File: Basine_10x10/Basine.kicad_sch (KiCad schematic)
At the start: 55 parts, among them J1 2060-451/998-404, J10 2060-451/998-404, J11 2060-451/998-404, J12 2060-451/998-404, J13 2060-451/998-404, J14 2060-451/998-404, J15 2060-451/998-404, J16 2060-451/998-404, J2 2060-451/998-404, J3 2060-451/998-404, J4 2060-451/998-404, J5 2060-451/998-404, J6 2060-451/998-404, J7 2060-451/998-404, J8 2060-451/998-404, J9 2060-451/998-404

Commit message: passage au pas de 2,54mm pour toutes les allumettes
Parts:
- removed TP1, TP10, TP11, TP12, TP2, TP3, TP4, TP5, TP6, TP7, TP8, TP9: TestPoint, Chimere_comps:Pastille, symbol Connector:TestPoint

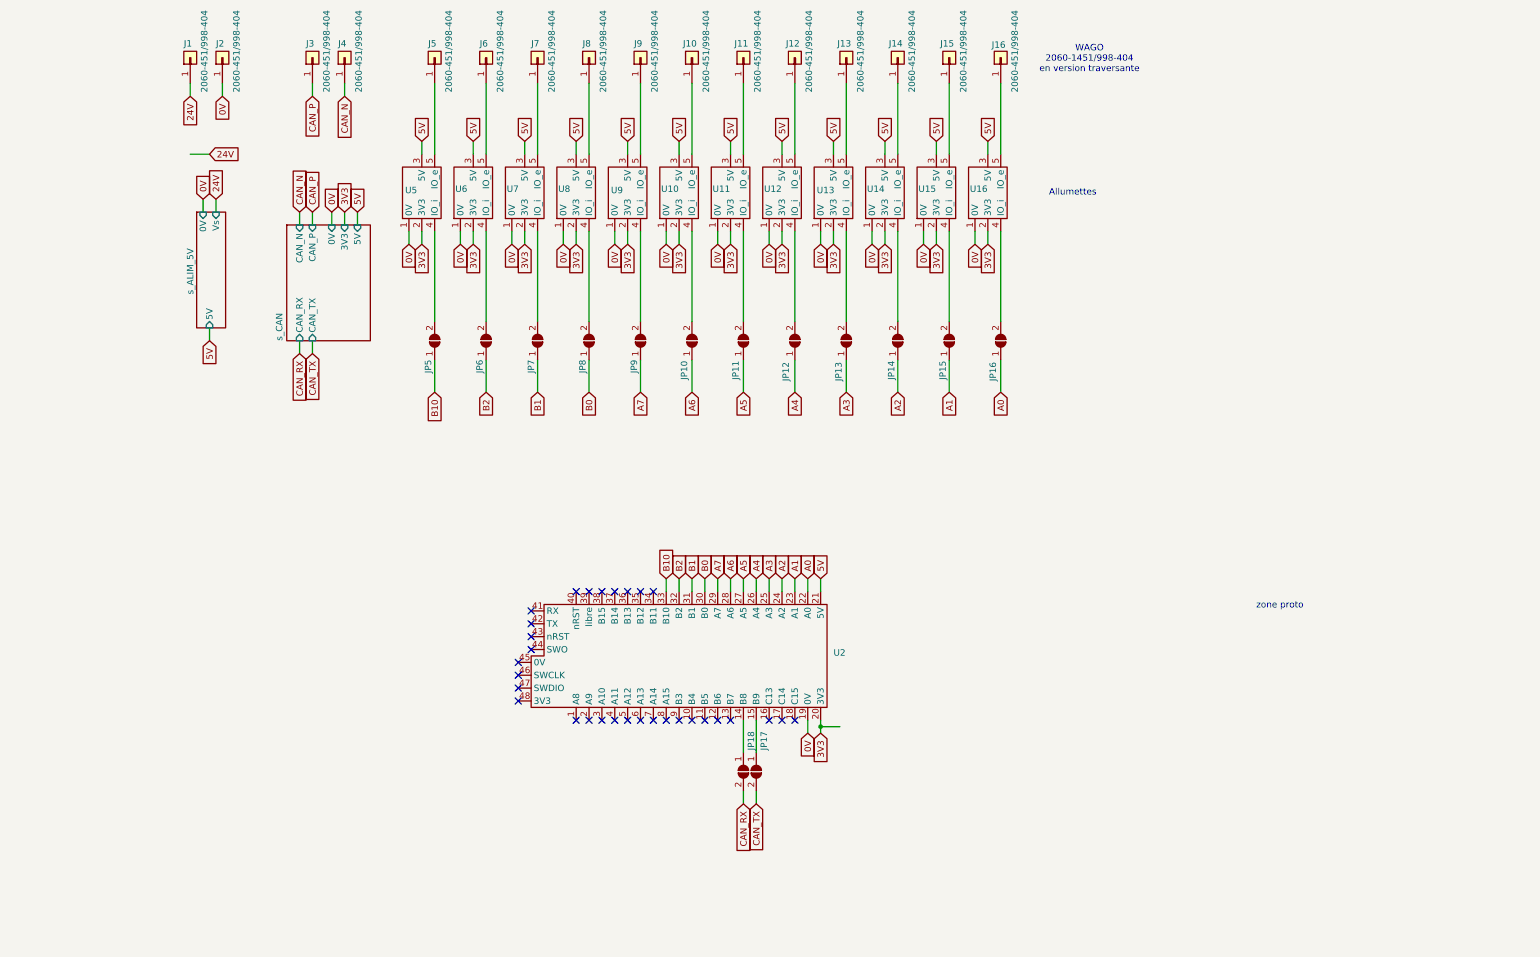
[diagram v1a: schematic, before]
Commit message: Basine 10x10 : enlever DCDC et CAN
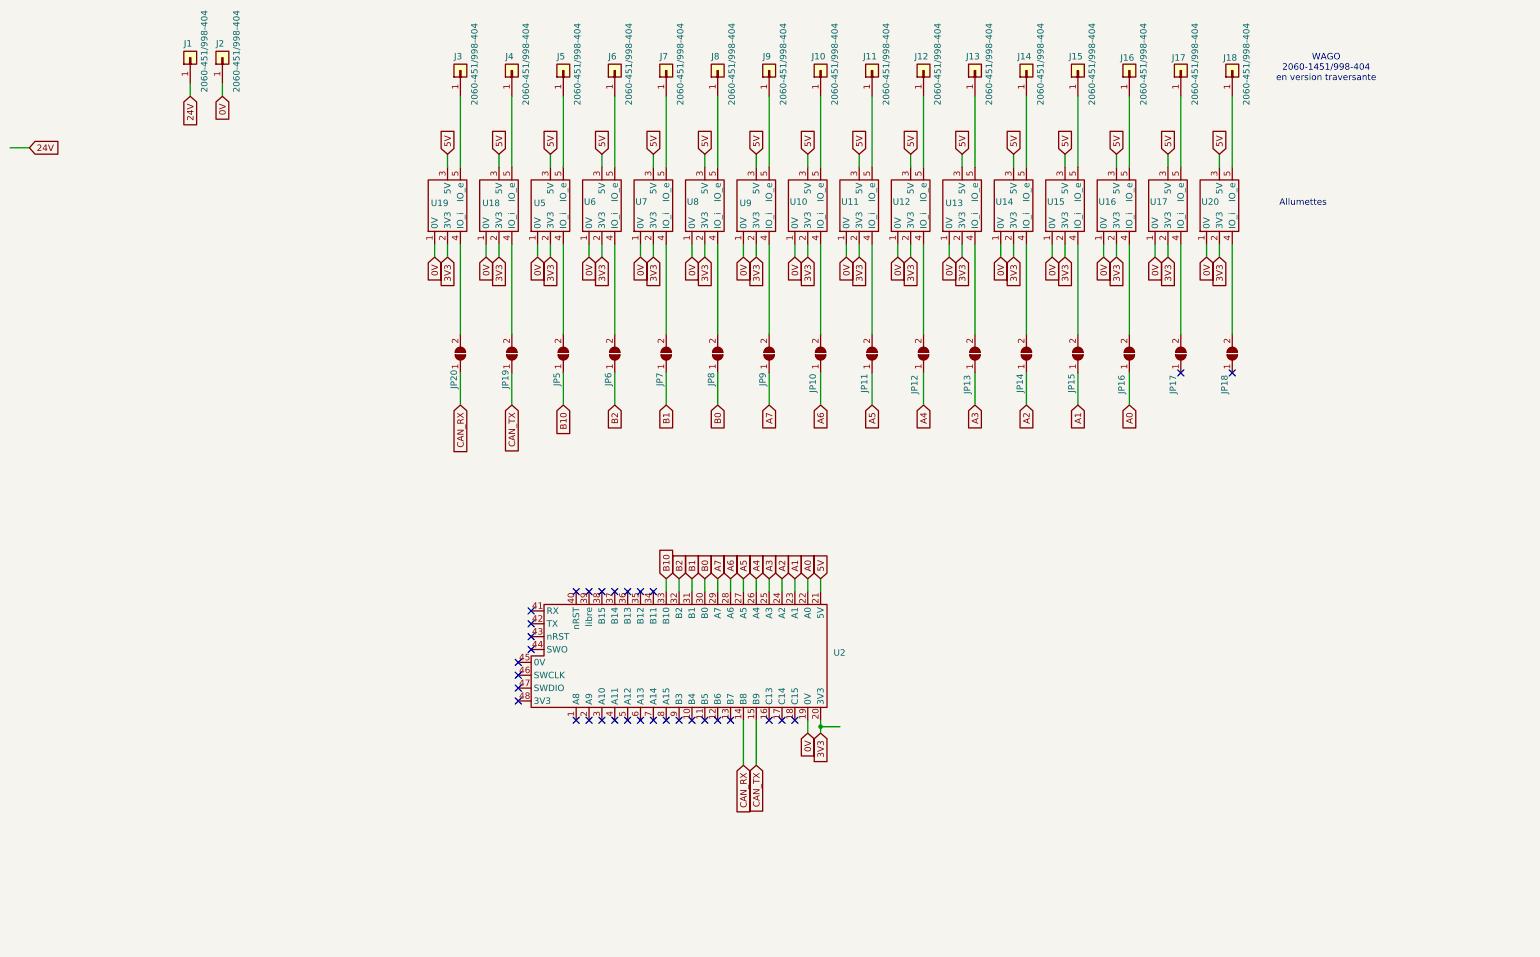
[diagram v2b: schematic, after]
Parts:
- added J17, J18: 2060-451/998-404, Chimere_comps:CONN_2060-1451_998-404_WAGO, symbol Connector_Generic:Conn_01x01
- added JP19, JP20: SolderJumper_2_Open, Jumper:SolderJumper-2_P1.3mm_Open_TrianglePad1.0x1.5mm, symbol Jumper:SolderJumper_2_Open
- added U17, U18, U19, U20: ~, Chimere_mods:Allumette, symbol Chimere_mods:Allumette
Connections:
- net 0V: now also U17.1 (0V), U18.1 (0V), U19.1 (0V), U20.1 (0V)
- net 3V3: now also U17.2 (3V3), U18.2 (3V3), U19.2 (3V3), U20.2 (3V3)
- net 5V: now also U17.3 (5V), U18.3 (5V), U19.3 (5V), U20.3 (5V)
- net CAN_RX: now also U2.14 (B8), JP20.1 (A); no longer JP18.2 (B)
- net CAN_TX: now also U2.15 (B9), JP19.1 (A); no longer JP17.2 (B)
- net at JP18.1 (A): no longer U2.14 (B8)
- net at JP17.1 (A): no longer U2.15 (B9)
- net CAN_N: no longer names the net of J4.1 (Pin_1)
- net CAN_N: now also U18.5 (IO_e)
- net CAN_P: no longer names the net of J3.1 (Pin_1)
- net CAN_P: now also U19.5 (IO_e)
- new net: JP17.2 (B), U17.4 (IO_i)
- new net: J17.1 (Pin_1), U17.5 (IO_e)
- new net: J18.1 (Pin_1), U20.5 (IO_e)
- new net: JP18.2 (B), U20.4 (IO_i)
- new net: JP20.2 (B), U19.4 (IO_i)
- new net: JP19.2 (B), U18.4 (IO_i)
- no-connect marks 31 -> 33
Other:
- removed sheet s_ALIM_5V
- removed sheet s_CAN
- note removed: "zone proto"
- moved on the sheet: J10, J11, J12, J13, J14, J15, J16, J3, J4, J5, J6, J7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

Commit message: Basine_10x10 : placement et routage
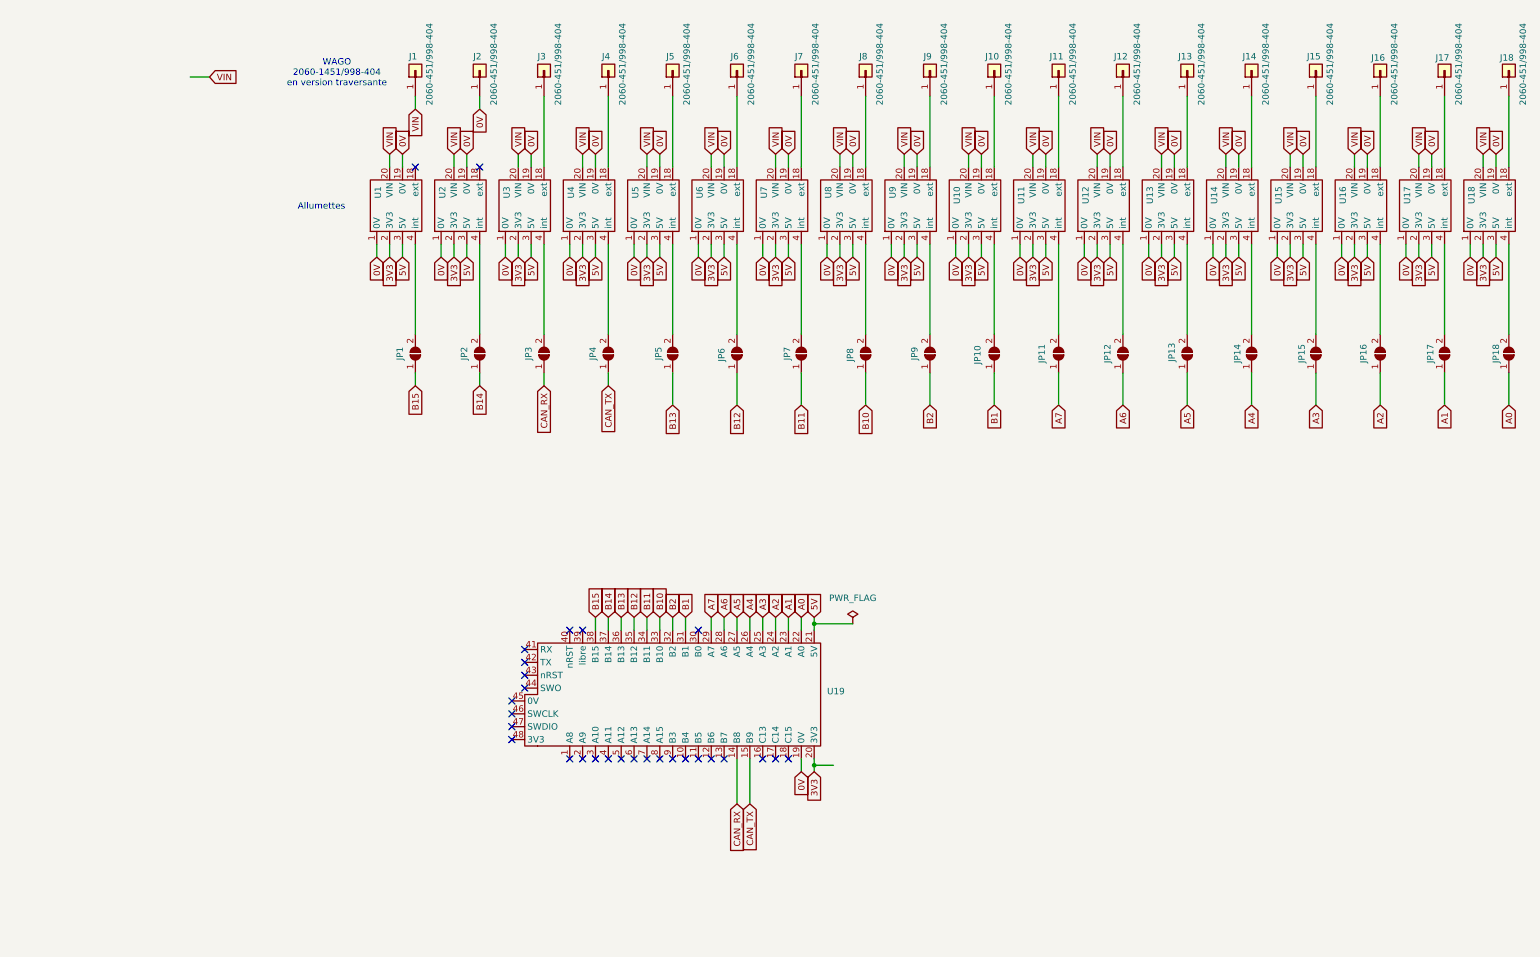
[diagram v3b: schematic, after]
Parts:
- removed U18, U19: ~, Chimere_mods:Allumette, symbol Chimere_mods:Allumette
- added JP1, JP2: SolderJumper_2_Open, Jumper:SolderJumper-2_P1.3mm_Open_TrianglePad1.0x1.5mm, symbol Jumper:SolderJumper_2_Open
- added U1, U2, U3, U4: ~, Chimere_mods:Allumette, symbol Chimere_mods:Allumette
- renumbered JP20 to JP3, JP19 to JP4, U20 to U18, U2 to U19
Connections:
- net 0V: now also U10.19 (0V), U11.19 (0V), U12.19 (0V), U13.19 (0V), U14.19 (0V), U15.19 (0V), U16.19 (0V), U17.19 (0V), U18.19 (0V), U5.19 (0V), U6.19 (0V), U7.19 (0V), U8.19 (0V), U9.19 (0V), U1.1 (0V), U1.19 (0V), U2.1 (0V), U2.19 (0V), U3.1 (0V), U3.19 (0V), U4.1 (0V), U4.19 (0V)
- net 3V3: now also U1.2 (3V3), U2.2 (3V3), U3.2 (3V3), U4.2 (3V3)
- net 5V: now also U1.3 (5V), U2.3 (5V), U3.3 (5V), U4.3 (5V)
- net A0: now also JP18.1 (A); no longer JP16.1 (A)
- net A1: now also JP17.1 (A); no longer JP15.1 (A)
- net A2: now also JP16.1 (A); no longer JP14.1 (A)
- net A3: now also JP15.1 (A); no longer JP13.1 (A)
- net A4: now also JP14.1 (A); no longer JP12.1 (A)
- net A5: now also JP13.1 (A); no longer JP11.1 (A)
- net A6: now also JP12.1 (A); no longer JP10.1 (A)
- net A7: now also JP11.1 (A); no longer JP9.1 (A)
- net B1: now also JP10.1 (A); no longer JP7.1 (A)
- net B10: now also JP8.1 (A); no longer JP5.1 (A)
- net B2: now also JP9.1 (A); no longer JP6.1 (A)
- net at J14.1 (Pin_1): now also U14.18 (ext); no longer U14.5 (IO_e)
- net at J3.1 (Pin_1): now also U3.18 (ext)
- net at J17.1 (Pin_1): now also U17.18 (ext); no longer U17.5 (IO_e)
- net B11: now reaches U19.34 (B11)
- net B11: now also JP7.1 (A)
- net B12: now reaches U19.35 (B12)
- net B12: now also JP6.1 (A)
- net B13: now reaches U19.36 (B13)
- net B13: now also JP5.1 (A)
- net B14: now reaches U19.37 (B14)
- net B14: now also JP2.1 (A)
- net B15: now reaches U19.38 (B15)
- net B15: now also JP1.1 (A)
- net at J18.1 (Pin_1): now also U18.18 (ext); no longer U18.5 (IO_e)
- net at J7.1 (Pin_1): now also U7.18 (ext); no longer U7.5 (IO_e)
- net at J11.1 (Pin_1): now also U11.18 (ext); no longer U11.5 (IO_e)
- net at JP3.2 (B): now also U3.4 (int)
- net at J12.1 (Pin_1): now also U12.18 (ext); no longer U12.5 (IO_e)
- net at J4.1 (Pin_1): now also U4.18 (ext)
- net at J9.1 (Pin_1): now also U9.18 (ext); no longer U9.5 (IO_e)
- net at J10.1 (Pin_1): now also U10.18 (ext); no longer U10.5 (IO_e)
- net at J5.1 (Pin_1): now also U5.18 (ext); no longer U5.5 (IO_e)
- net at J16.1 (Pin_1): now also U16.18 (ext); no longer U16.5 (IO_e)
- net at J13.1 (Pin_1): now also U13.18 (ext); no longer U13.5 (IO_e)
- net at J6.1 (Pin_1): now also U6.18 (ext); no longer U6.5 (IO_e)
- net at J8.1 (Pin_1): now also U8.18 (ext); no longer U8.5 (IO_e)
- net at J15.1 (Pin_1): now also U15.18 (ext); no longer U15.5 (IO_e)
- net at JP4.2 (B): now also U4.4 (int)
- net 24V renamed VIN
- net VIN: now also U10.20 (VIN), U11.20 (VIN), U12.20 (VIN), U13.20 (VIN), U14.20 (VIN), U15.20 (VIN), U16.20 (VIN), U17.20 (VIN), U18.20 (VIN), U5.20 (VIN), U6.20 (VIN), U7.20 (VIN), U8.20 (VIN), U9.20 (VIN), U1.20 (VIN), U2.20 (VIN), U3.20 (VIN), U4.20 (VIN)
- net B0: no longer names the net of U19.30 (B0)
- net B0: no longer JP8.1 (A)
- new net: JP1.2 (B), U1.4 (int)
- new net: JP2.2 (B), U2.4 (int)
- no-connect marks 33 -> 29
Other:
- moved on the sheet: J1, J10, J11, J12, J13, J14, J15, J16, J17, J18, J2, J3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

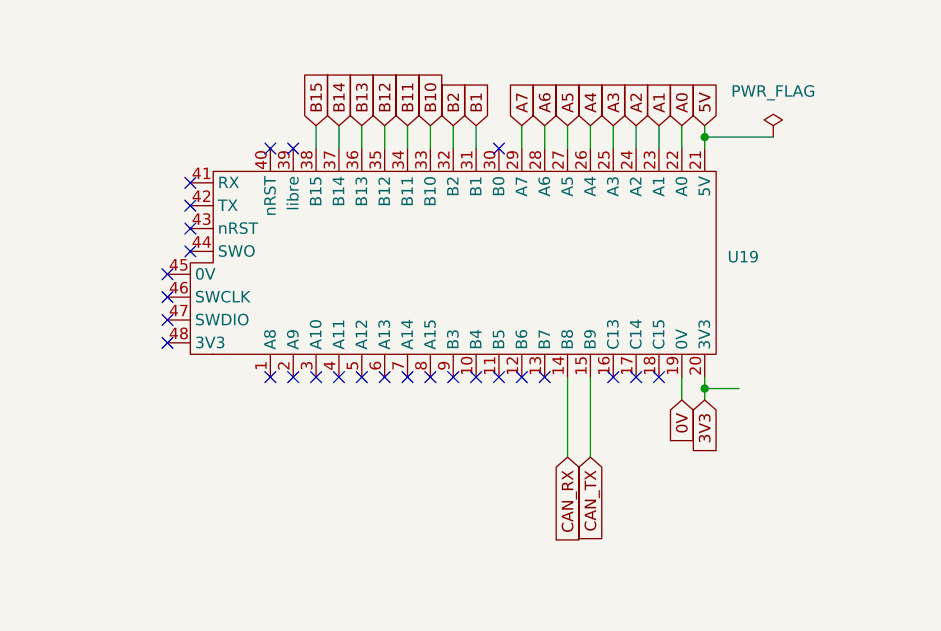
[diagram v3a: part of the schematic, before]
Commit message: Basine 10x10: modification ultrogothe, allumettes, 3v3 en option
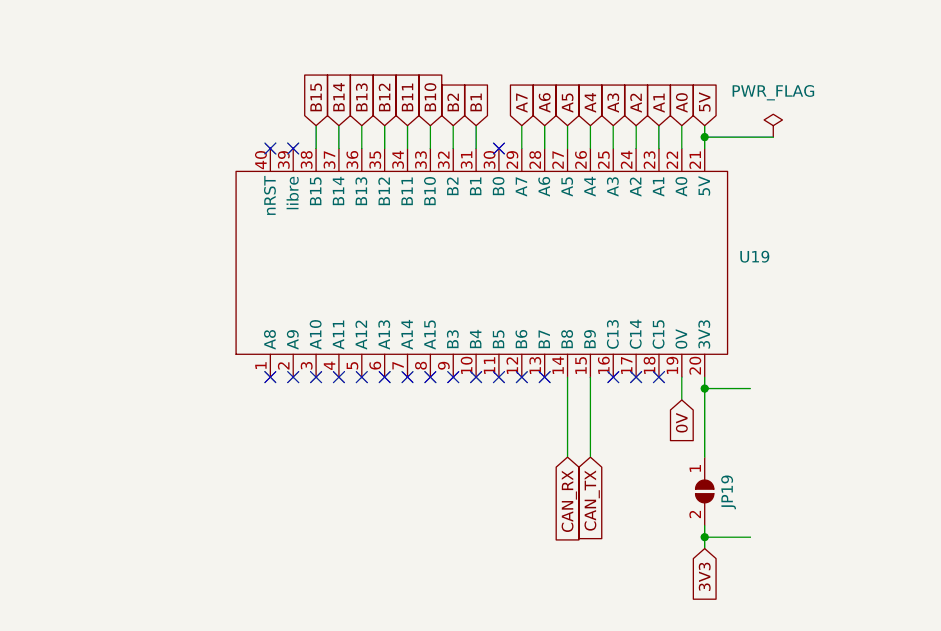
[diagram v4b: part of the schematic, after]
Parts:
- added JP19: SolderJumper_2_Open, Jumper:SolderJumper-2_P1.3mm_Open_TrianglePad1.0x1.5mm, symbol Jumper:SolderJumper_2_Open
- J1, J10, J11, J12, J13, J14, J15, J16, J17, J18, J2, J3, J4, J5, J6, J7, J8, J9: footprint Chimere_comps:CONN_2060-1451_998-404_WAGO -> Chimere_comps:Conn_bornier_et_wago
- U1, U10, U11, U12, U13, U14, U15, U16, U17, U18, U19, U2, U3, U4, U5, U6, U7, U8, U9: now in the parts list
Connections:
- net 3V3: now also JP19.2 (B); no longer U19.20 (3V3)
- new net: JP19.1 (A), U19.20 (3V3)
- no-connect marks 29 -> 21
